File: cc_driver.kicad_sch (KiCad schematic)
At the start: 31 parts, among them IC2 TPS922053DRRR, IC3 TPS922053DRRR, J3 LED_OUT

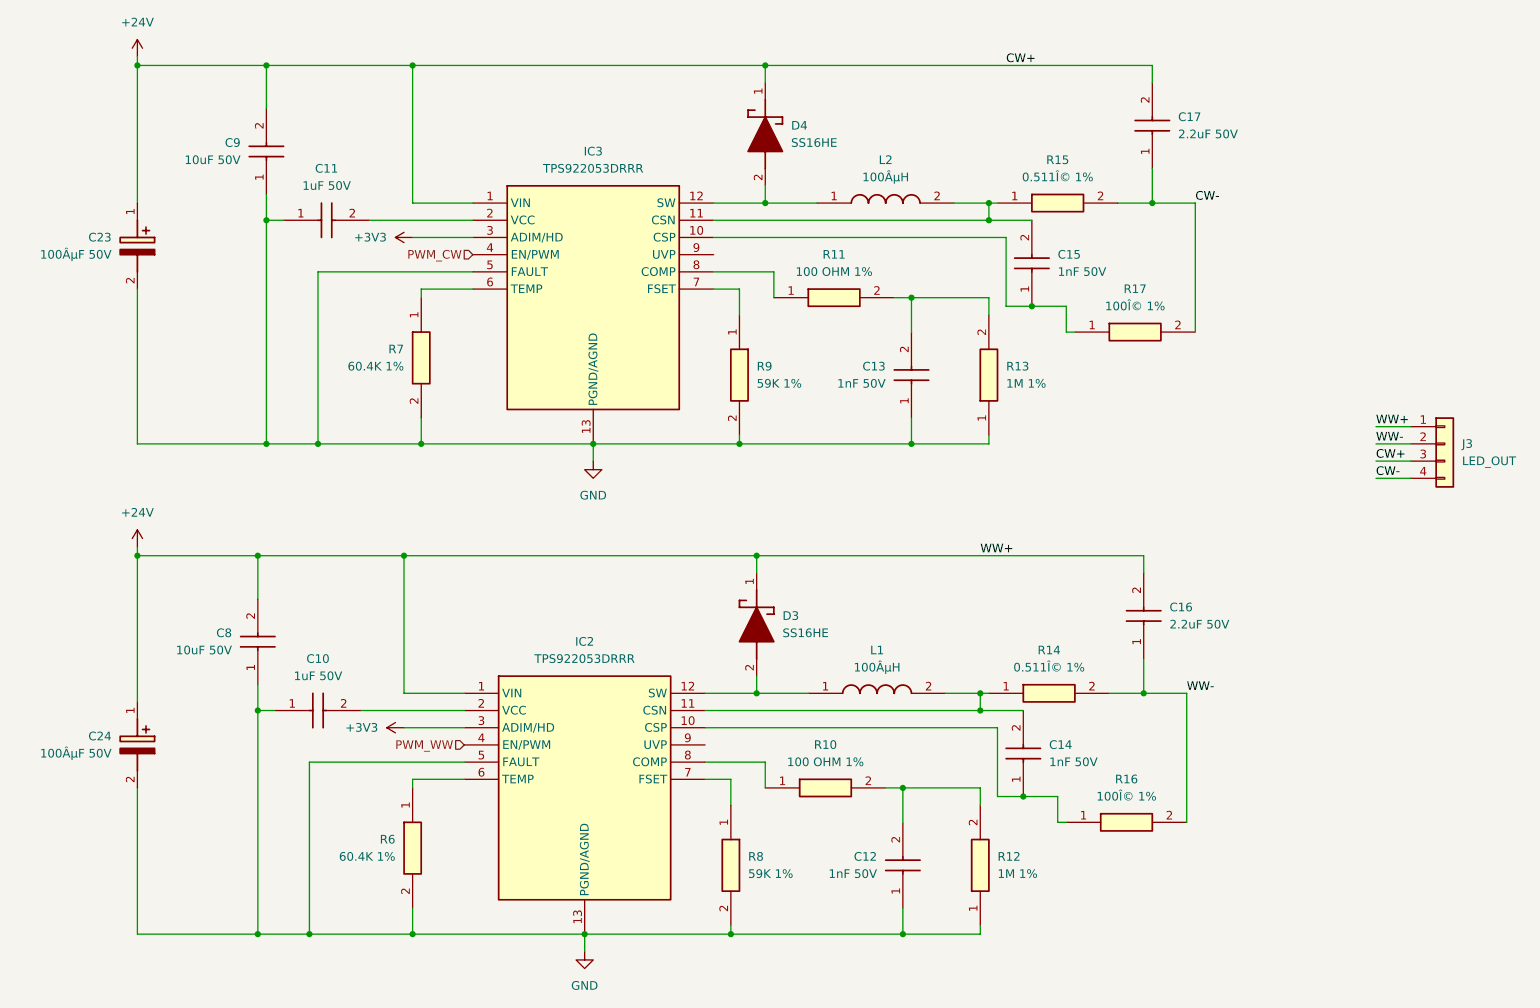
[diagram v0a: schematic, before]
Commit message: Finalize KiCad PCB sources for 5-piece test build
Commit the completed Open Vettam 15CCT KiCad source design files prepared for the initial five-piece production test run.

Included files are limited to the schematic hierarchy, PCB layouts, KiCad project files, and the LED MCPCB design-rules file. Generated BOM exports, fabrication output archives, freerouting/temp files, logs, backups, images, netlists, and Altium import artifacts are intentionally left unstaged.

Updated main controller board sources:

- open_vettam_15CCT.kicad_sch

- open_vettam_15CCT.kicad_pcb

- open_vettam_15CCT.kicad_pro

- 24v_Input.kicad_sch

- 24-5_buck.kicad_sch

- MCU.kicad_sch

- cc_driver.kicad_sch

Updated LED MCPCB sources:

- led_mcpcb/led_mcpcb.kicad_sch

- led_mcpcb/led_mcpcb.kicad_pcb

- led_mcpcb/led_mcpcb.kicad_pro

- led_mcpcb/led_mcpcb.kicad_dru

- led_mcpcb/CW-5000.kicad_sch

- led_mcpcb/WW-3000.kicad_sch

- led_mcpcb/digital_temp.kicad_sch
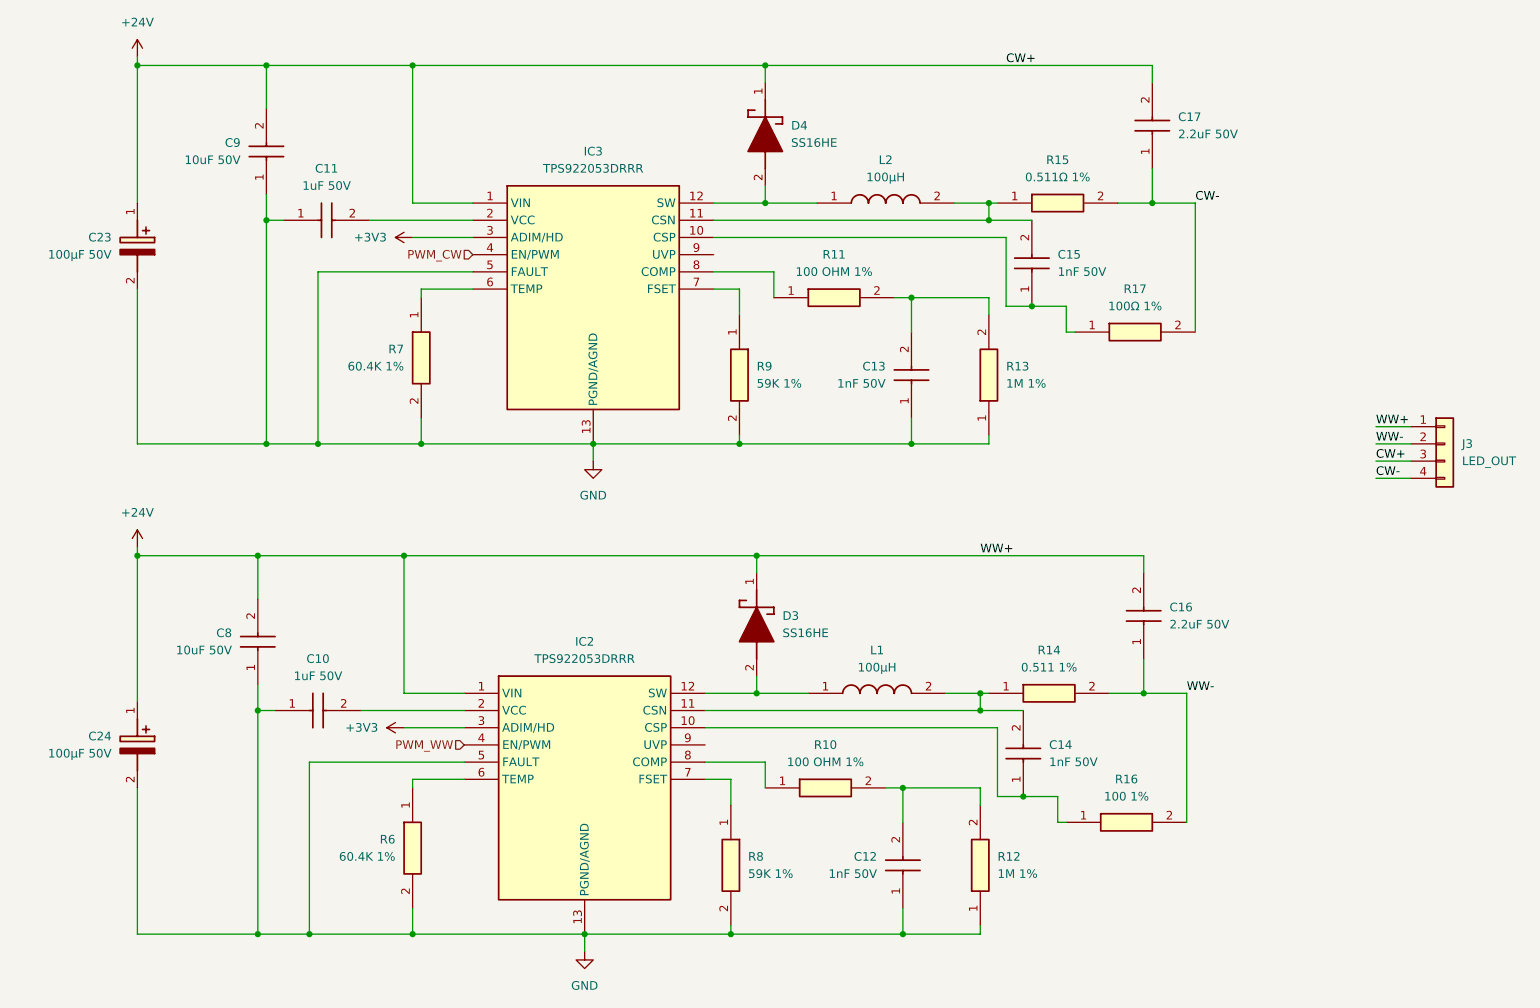
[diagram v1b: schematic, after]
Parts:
- C23, C24: value 100ÂµF 50V -> 100µF 50V
- L1, L2: value 100ÂµH -> 100µH
- R14: value 0.511Î© 1% -> 0.511 1%
- R15: value 0.511Î© 1% -> 0.511Ω 1%
- R16: value 100Î© 1% -> 100 1%
- R17: value 100Î© 1% -> 100Ω 1%
